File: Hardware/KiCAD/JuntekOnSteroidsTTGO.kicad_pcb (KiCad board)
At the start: 2 copper layers, 54 x 36.8 mm, 30 parts, among them J1 To PSU host board, J2 To PSU host board, J3 Serial, J4 ESP32-TFT, J5 ESP32-TFT, J6 I2C, J7 PWR, J8 Conn_02x12_Odd_Even

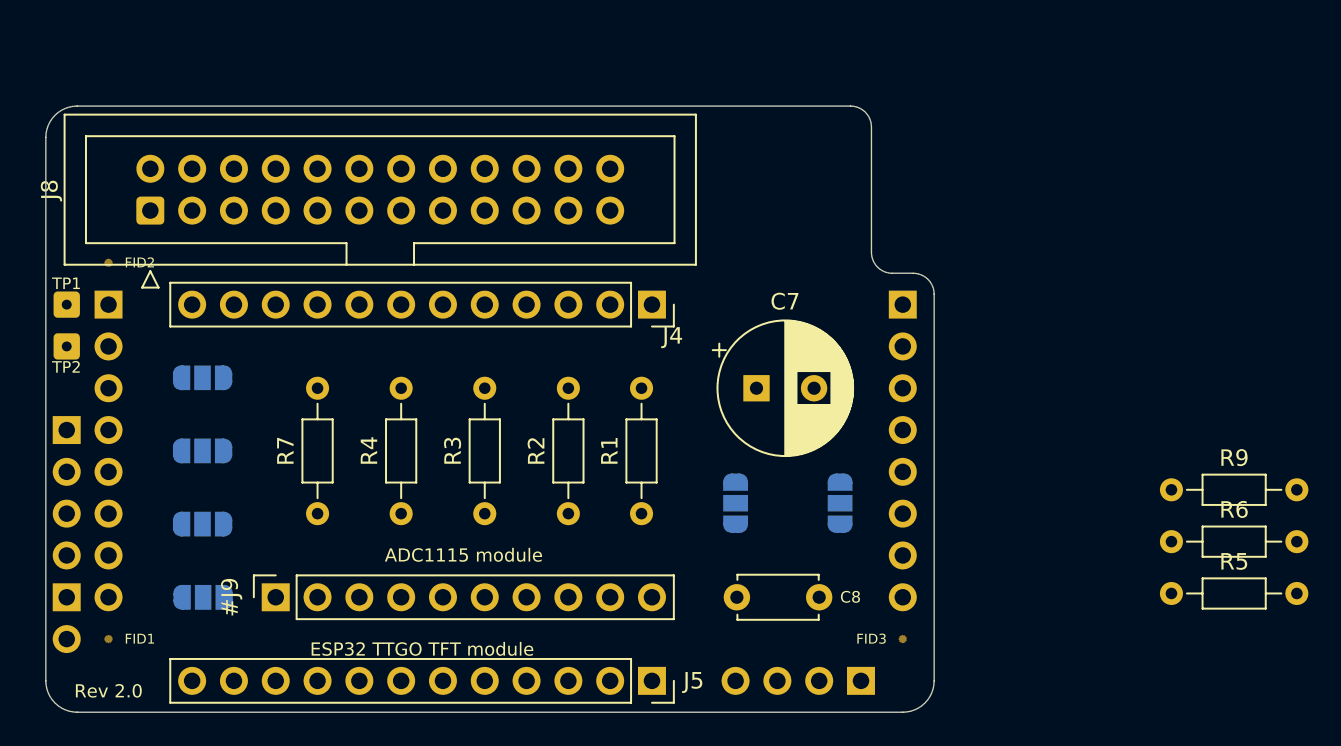
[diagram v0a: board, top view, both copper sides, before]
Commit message: Change exp. connector, add ADC caps
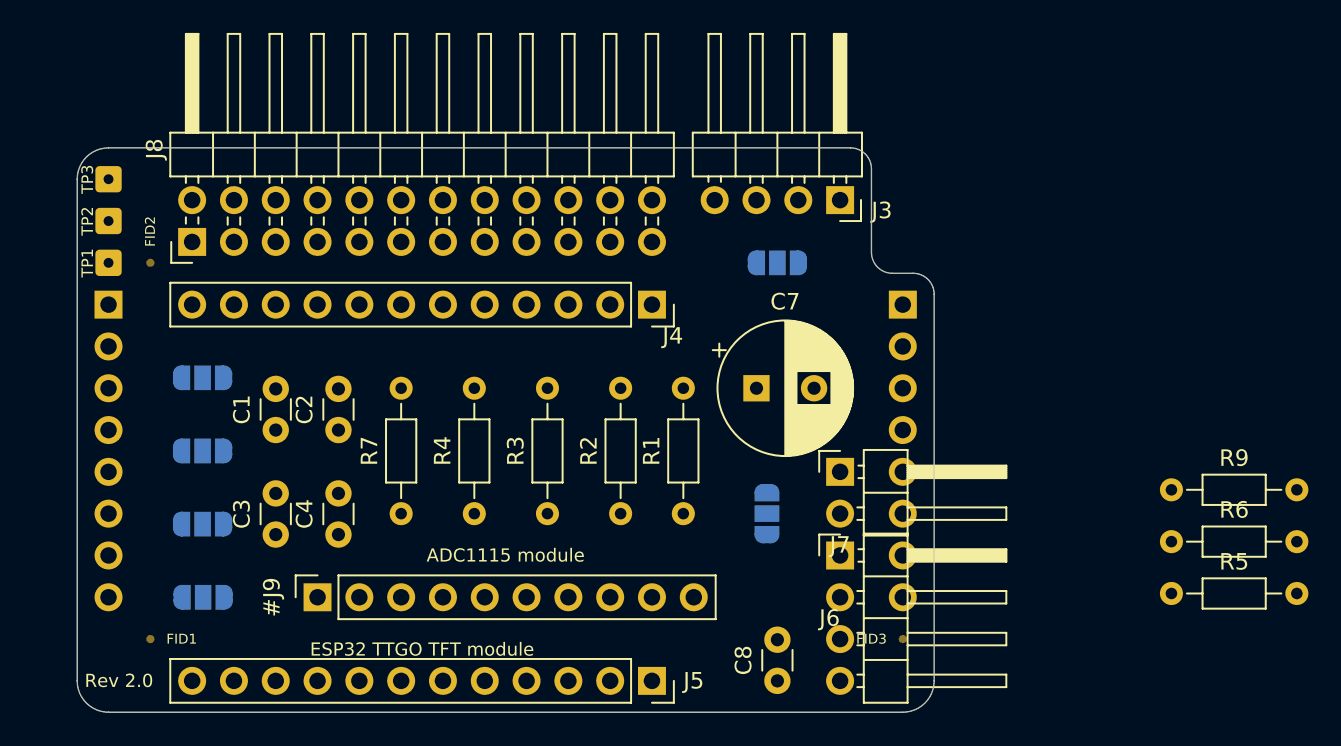
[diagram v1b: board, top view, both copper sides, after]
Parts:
- added C1: 0.1µ, Capacitor_THT:C_Disc_D3.0mm_W1.6mm_P2.50mm, F.Cu at (113.7, 75.6)
- added C2: 0.1µ, Capacitor_THT:C_Disc_D3.0mm_W1.6mm_P2.50mm, F.Cu at (117.5, 75.6)
- added C3: 0.1µ, Capacitor_THT:C_Disc_D3.0mm_W1.6mm_P2.50mm, F.Cu at (113.7, 81.9)
- added C4: 0.1µ, Capacitor_THT:C_Disc_D3.0mm_W1.6mm_P2.50mm, F.Cu at (117.5, 81.9)
- added TP3: ADC2, Connector_Wire:SolderWire-0.1sqmm_1x01_D0.4mm_OD1mm, F.Cu at (103.5, 60.3)
- C8: footprint Capacitor_THT:C_Disc_D4.7mm_W2.5mm_P5.00mm -> Capacitor_THT:C_Disc_D3.0mm_W1.6mm_P2.50mm
- J3, J6, J7: moved to F.Cu
- J8: footprint Connector_IDC:IDC-Header_2x12_P2.54mm_Vertical -> Connector_PinHeader_2.54mm:PinHeader_2x12_P2.54mm_Horizontal
- moved J6 47.6 mm to (148.0, 83.2), turned to 0 degrees
- moved J7 47.6 mm to (148.0, 78.1), turned to 0 degrees
- moved J3 29.2 mm to (140.3, 61.6), turned to 90 degrees
- moved JP6 14.8 mm to (144.1, 65.4), turned to 0 degrees
- moved TP2 8.03 mm to (103.5, 62.9)
- moved C8 5.68 mm to (144.1, 90.8), turned to 90 degrees
- moved R7 5.08 mm to (121.3, 80.6)
- moved JP1 4.49 mm to (143.5, 80.6)
- moved R4 4.45 mm to (125.7, 80.6)
- moved R3 3.81 mm to (130.2, 80.6)
- moved TP1 3.59 mm to (103.5, 65.4)
- moved R2 3.18 mm to (134.6, 80.6)
- moved J8 3.17 mm to (108.6, 64.1)
- moved R1 2.54 mm to (138.4, 80.6)
- moved FID1 2.54 mm to (106.0, 88.3)
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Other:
- board size 54 x 36.8 mm -> 52.1 x 34.3 mm

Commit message: v2.2
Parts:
- removed J3: Serial, Connector_PinHeader_2.54mm:PinHeader_1x04_P2.54mm_Horizontal
- removed J8: Conn_02x12_Odd_Even, Connector_PinHeader_2.54mm:PinHeader_2x12_P2.54mm_Horizontal
- removed JP2: Vin_sense, Jumper:SolderJumper-3_P1.3mm_Open_RoundedPad1.0x1.5mm
- removed R3, R4, R5, R6, R9: 3M8, Resistor_THT:R_Axial_DIN0204_L3.6mm_D1.6mm_P7.62mm_Horizontal
- removed TP1: ADC0, Connector_Wire:SolderWire-0.1sqmm_1x01_D0.4mm_OD1mm
- removed TP2: ADC1, Connector_Wire:SolderWire-0.1sqmm_1x01_D0.4mm_OD1mm
- removed TP3: ADC2, Connector_Wire:SolderWire-0.1sqmm_1x01_D0.4mm_OD1mm
- added J11: Expansion1, Connector_PinHeader_2.54mm:PinHeader_1x12_P2.54mm_Horizontal, B.Cu at (113.7, 90.8)
- added J12: Expansion2, Connector_PinHeader_2.54mm:PinHeader_1x12_P2.54mm_Horizontal, B.Cu at (113.7, 88.3)
- added JP1001: SolderJumper_2_Open, Jumper:SolderJumper-2_P1.3mm_Open_RoundedPad1.0x1.5mm, B.Cu at (141.6, 82.5)
- added JP1002: SolderJumper_2_Open, Jumper:SolderJumper-2_P1.3mm_Open_RoundedPad1.0x1.5mm, B.Cu at (141.6, 85.1)
- added R1001: 10k/none, Resistor_THT:R_Axial_DIN0204_L3.6mm_D1.6mm_P7.62mm_Horizontal, F.Cu at (135.9, 73.0)
- added R1002: 2k2/none, Resistor_THT:R_Axial_DIN0204_L3.6mm_D1.6mm_P7.62mm_Horizontal, F.Cu at (120.0, 65.4)
- added R1003: 1k/zero, Resistor_THT:R_Axial_DIN0204_L3.6mm_D1.6mm_P7.62mm_Horizontal, F.Cu at (123.2, 65.4)
- added R14: 1k/zero, Resistor_THT:R_Axial_DIN0204_L3.6mm_D1.6mm_P7.62mm_Horizontal, F.Cu at (116.8, 73.0)
- added R15: 100k/none, Resistor_THT:R_Axial_DIN0204_L3.6mm_D1.6mm_P7.62mm_Horizontal, F.Cu at (132.7, 73.0)
- J6: value I2C -> feedback; footprint Connector_PinHeader_2.54mm:PinHeader_1x04_P2.54mm_Horizontal -> Connector_PinHeader_2.54mm:PinHeader_1x03_P2.54mm_Horizontal; moved to B.Cu
- J7: value PWR -> I2C; footprint Connector_PinHeader_2.54mm:PinHeader_1x02_P2.54mm_Horizontal -> Connector_JST:JST_PH_B4B-PH-K_1x04_P2.00mm_Vertical
- JP3: value Vin_sense -> VinSense
- JP4: value Vin_sense -> Iout_sense
- JP5: value Vin_sense -> VoutSense
- JP6: value Vin_sense -> FanPWM
- R11: renamed from R2; value 3M8 -> 68k/zero
- R12: renamed from R7; value 3M8 -> 68k/zero
- R17: renamed from R1; value 3M8 -> 1k
- moved J6 45.1 mm to (103.5, 90.8), turned to 270 degrees
- moved JP6 42.9 mm to (106.0, 85.1), turned to 90 degrees
- moved JP5 16.9 mm to (113.0, 69.2)
- moved C8 14.1 mm to (139.7, 77.5), turned to 270 degrees
- moved C2 12.5 mm to (106.7, 69.2), turned to 0 degrees
- moved C3 12.3 mm to (106.7, 71.8), turned to 0 degrees
- moved J7 12.1 mm to (146.7, 90.2), turned to 90 degrees
- moved C1 11.3 mm to (106.7, 66.7), turned to 0 degrees
- moved R11 11.2 mm to (126.4, 73.0)
- moved R12 11.2 mm to (129.5, 73.0)
- moved JP4 10.9 mm to (113.0, 66.7)
- moved JP3 10.3 mm to (113.0, 71.8)
- moved JP1 9.94 mm to (148.0, 71.8)
- moved #J9 9.16 mm to (111.1, 78.1)
- moved C4 9.03 mm to (110.5, 87.6), turned to 180 degrees
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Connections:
- net Net-(C4-Pad1) renamed /IloadSense
- net Net-(R1-Pad2) renamed /Shunt
- C1 pad 1: Net-(C1-Pad1) -> /J1.1
- C1 pad 2: Net-(C1-Pad2) -> /GND
- C2 pad 1: Net-(C2-Pad1) -> /J1.2
- C2 pad 2: Net-(C2-Pad2) -> /GND
- C3 pad 1: Net-(C3-Pad1) -> /J1.3
- C3 pad 2: Net-(C3-Pad2) -> /GND
- C4 pad 2: Net-(C4-Pad2) -> /GND
- J1 pad 1: Net-(J1-Pad1) -> /J1.1
- J1 pad 2: Net-(J1-Pad2) -> /J1.2
- J1 pad 3: Net-(J1-Pad3) -> /J1.3
- J1 pad 4: Net-(J1-Pad4) -> /J1.4
- J1 pad 5: Net-(J1-Pad5) -> /J1.5
- J1 pad 6: Net-(J1-Pad6) -> /J1.6
- J1 pad 7: Net-(J1-Pad7) -> /ADC2
- J1 pad 8: Net-(J1-Pad8) -> /J1.8
- J4 pad 12: +3V3 -> /+3V3
- J5 pad 1: +3V3 -> /+3V3
- J6 pad 1: /SCL -> /ADC2
- J6 pad 2: /SDA -> /A3
- J6 pad 3: +3V3 -> /GPIO12
- J7 pad 1: /GND -> /SCL
- J7 pad 2: VCC -> /SDA
- JP3 pad 1: Net-(JP3-Pad1) -> /A2
- JP3 pad 2: Net-(JP3-Pad2) -> /J1.3
- JP3 pad 3: Net-(JP3-Pad3) -> /ADC1
- JP4 pad 1: Net-(JP4-Pad1) -> /A0
- JP4 pad 2: Net-(JP4-Pad2) -> /J1.1
- JP4 pad 3: Net-(JP4-Pad3) -> /ADC3
- JP5 pad 1: Net-(JP5-Pad1) -> /A1
- JP5 pad 2: Net-(JP5-Pad2) -> /J1.2
- JP5 pad 3: Net-(JP5-Pad3) -> /ADC0
- JP6 pad 1: Net-(JP6-Pad1) -> /J1.8
- JP6 pad 3: Net-(JP6-Pad3) -> /ADC2
- R11 pad 1: Net-(R2-Pad1) -> /J1.5
- R11 pad 2: Net-(R2-Pad2) -> /GPIO32
- R12 pad 1: Net-(R7-Pad1) -> /J1.4
- R12 pad 2: Net-(R7-Pad2) -> /GPIO33
- R17 pad 1: Net-(R1-Pad1) -> /A3
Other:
- outline, holes or cut-outs redrawn
- board text added: "Rev 2.2"
- board text removed: "Rev 2.0"

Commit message: v2.2 and a bit
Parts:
- added R1004: 100k/zero, Resistor_THT:R_Axial_DIN0204_L3.6mm_D1.6mm_P7.62mm_Horizontal, F.Cu at (142.2, 69.8)
- added R1005: 1k/none, Resistor_THT:R_Axial_DIN0204_L3.6mm_D1.6mm_P7.62mm_Horizontal, F.Cu at (148.6, 62.2)
- R17: value 1k -> 1k/zero
- moved JP1 2.29 mm to (149.2, 73.7)
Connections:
- J6 pad 1: /ADC2 -> /J6.1
- J6 pad 2: /A3 -> /J6.2
- R17 pad 2: /Shunt -> /J6.2
